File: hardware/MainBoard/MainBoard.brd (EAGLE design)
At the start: 90 x 56 mm, 220 parts, among them J1 CON-71741-2184-BOT, J2 CON-71741-2184-TOP, J3 CON-FTSH-105-01-L-DV-K, J4 CON-ZX62R-B-5P, J5 CON-SMA, J6 CON-SMA, J7 CON-RJ45-J0G-0007NL, J8 SWITCH-CJS-1200-1200, M1 MOUNT-HOLE3.3, M2 MOUNT-HOLE3.3, M3 MOUNT-HOLE3.3, M4 MOUNT-HOLE3.3, M5 FIDUCIAL1X2, M6 FIDUCIAL1X2, M7 FIDUCIAL1X2, M8 FIDUCIAL1X2, Q1 MMBT3904, SW1 SWITCH-KSC-201J, SW2 SWITCH-KSC-201J, U1 A2F500M3G-FG256, U2 MAX19706-T4877-4, U3 MAX19706-T4877-4, U4 USBLC6-2SC6, U5 FT232HL, U6 DP83848C-VBH48A, U7 93LC56BT-OT, U8 DS1818-10-SOT-23, U9 LMV112, X1 FOX924B, X2 ECX-31B, X3 ASEM1-C, X5 ECX-42-120

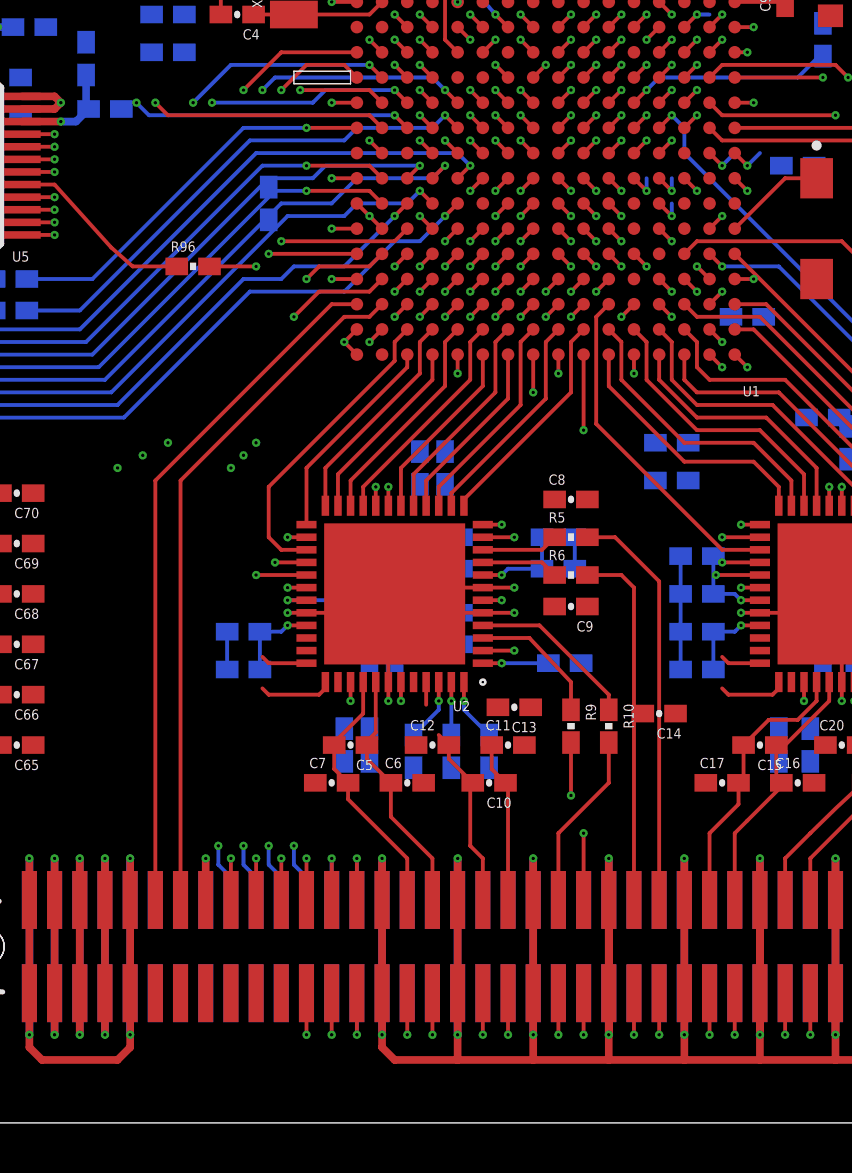
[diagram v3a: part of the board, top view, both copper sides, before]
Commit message: 
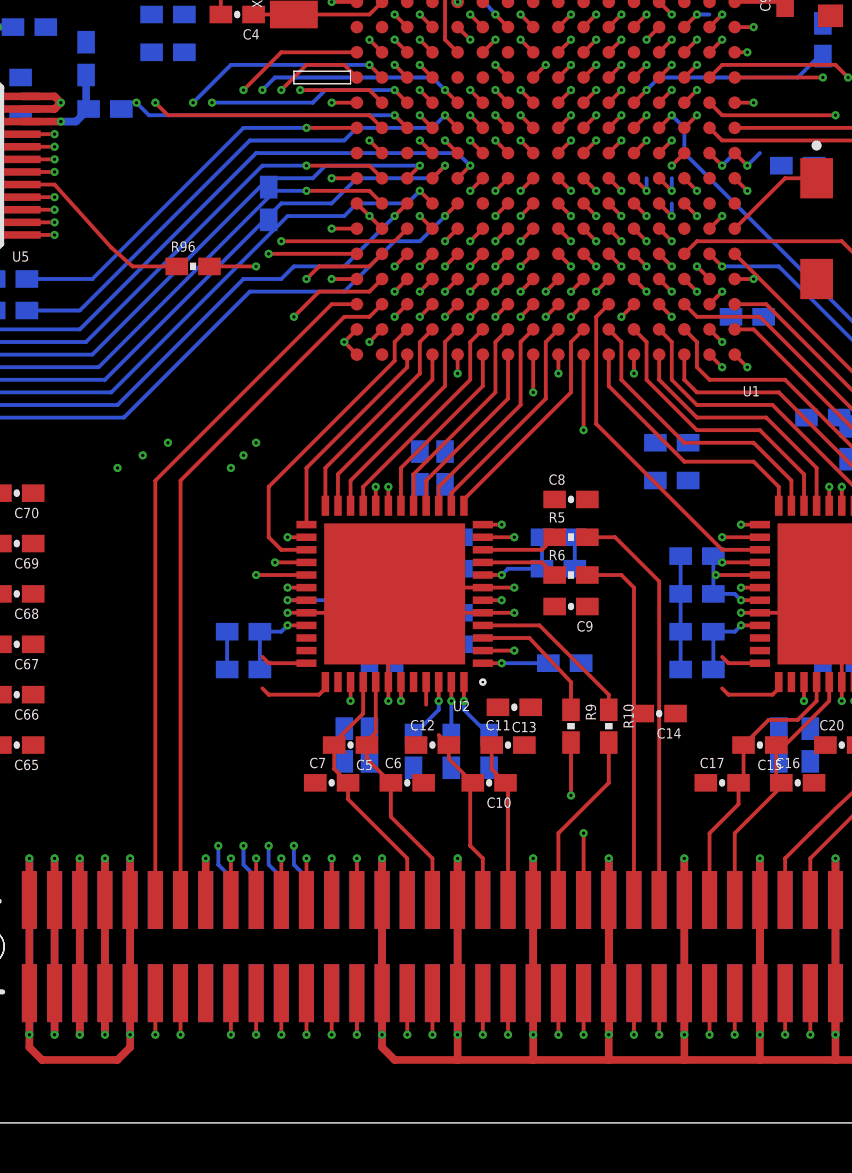
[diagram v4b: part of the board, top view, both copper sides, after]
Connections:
- removed net N$6: U1.G5
- net NGPIO0: now also U1.J3
- net NGPIO1: now also U1.H2
- net NGPIO2: now also U1.G1
- net NGPIO3: now also U1.G3
- net NGPIO4: now also U1.G2
- net SGPIO0: now also U1.E4
- net SGPIO1: now also U1.F5
- net SGPIO2: now also U1.D5
- net SGPIO3: now also U1.G5
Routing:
- net NGPIO0: track 0.00 -> 6.39 mm, vias 0 -> 2
- net NGPIO2: track 0.00 -> 5.19 mm, vias 0 -> 1
- net NGPIO1: track 0.00 -> 5.19 mm, vias 0 -> 1
- net NGPIO3: track 0.00 -> 4.98 mm, vias 0 -> 2
- net NGPIO4: track 0.00 -> 3.77 mm, vias 0 -> 1
- net SGPIO3: track 0.00 -> 1.21 mm, vias 0 -> 1
- net SGPIO2: track 0.00 -> 1.21 mm, vias 0 -> 1
- net SGPIO1: track 0.00 -> 1.21 mm, vias 0 -> 1
- net SGPIO0: track 0.00 -> 1.21 mm, vias 0 -> 1

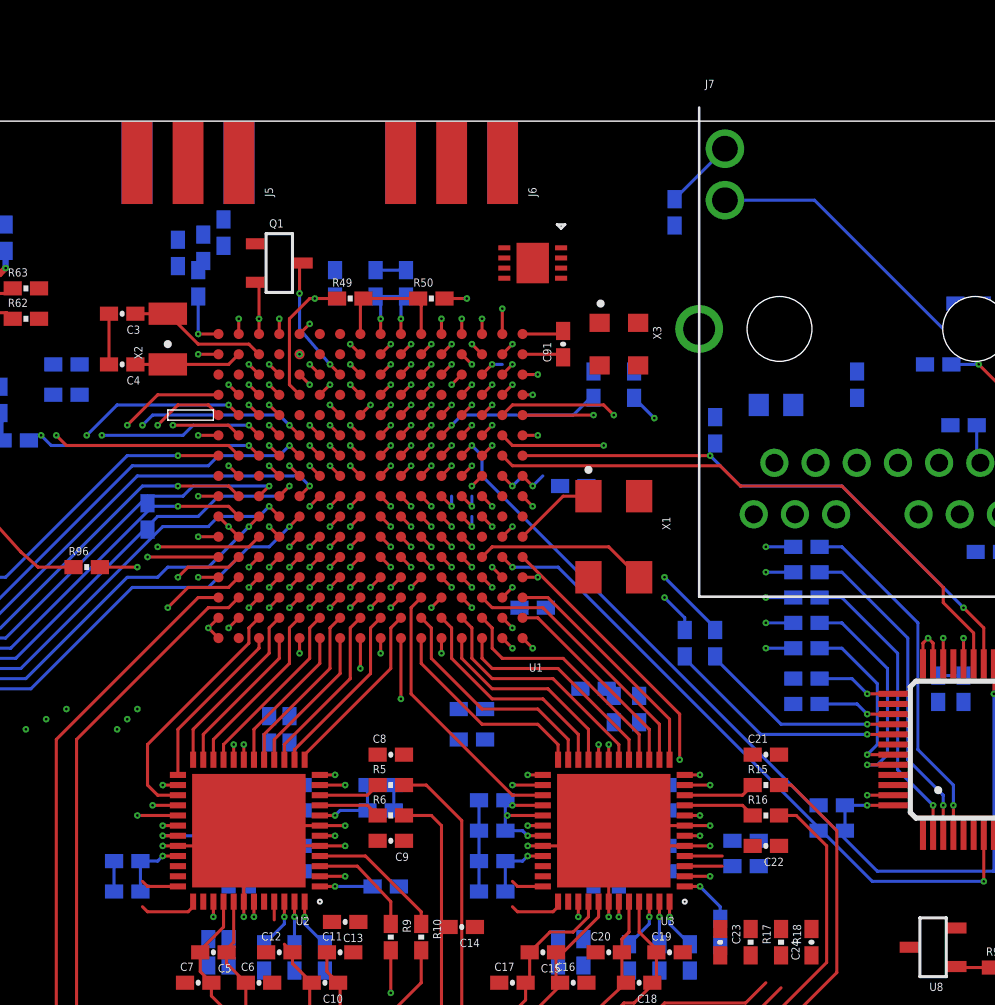
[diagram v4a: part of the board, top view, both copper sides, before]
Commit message: Routed external clocks (still needs adjustment).
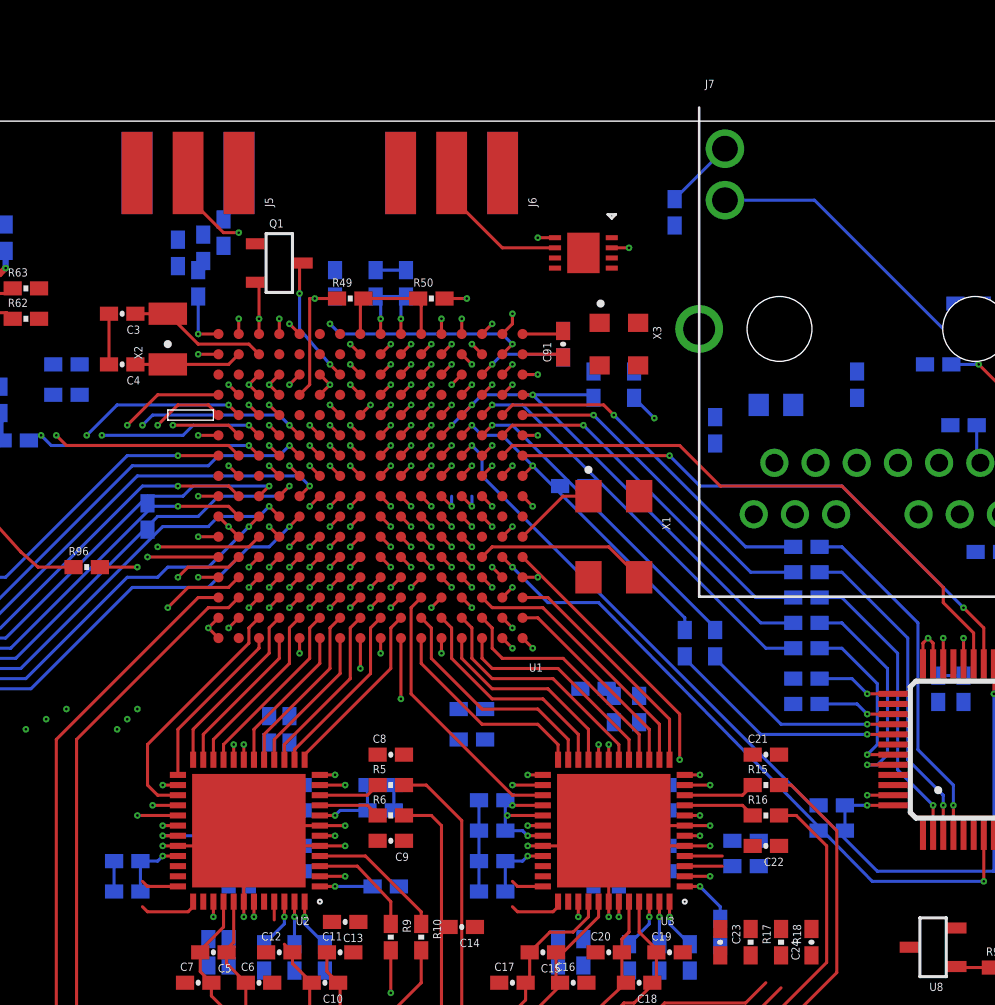
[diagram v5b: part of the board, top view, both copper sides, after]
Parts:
- moved C109 13.1 mm to (54.5, 45.0), turned to 90 degrees
- moved U9 2.55 mm to (55.5, 49.5)
- moved J5 0.50 mm to (36.0, 55.5)
- moved J6 0.50 mm to (49.0, 55.5)
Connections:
- net D3V3: no longer C74.1, C75.1, C76.1
- net VJTAG: now also C74.1
- net VPUMP: now also C75.1, C76.1
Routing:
- net EXT_CLK_IN: track 1.21 -> 30.2 mm, vias 1 -> 2
- net EXT_CLK_OUT: track 1.41 -> 14.2 mm, vias 1 -> 2
- net EXT_CLK_OUT_EN: track 1.41 -> 13.3 mm, vias 1 -> 2
- net EXT_CLK_OUT_BUF: track 0.00 -> 7.33 mm
- net VCC3N: track 1.21 -> 4.48 mm
- net SF_DAC1: track 46.5 -> 45.5 mm
- net SF_DAC0: track 54.5 -> 55.3 mm
- net SF_ABPS1: track 52.1 -> 51.4 mm
- net SF_CM0: track 50.2 -> 49.6 mm
- net MAC_TXEN: track 17.7 -> 18.1 mm, vias 2 -> 1
- net MAC_TXD1: vias 2 -> 1
- net MAC_TXD0: vias 2 -> 1
- net MAC_RXER: vias 2 -> 1
- net MAC_RXD1: vias 2 -> 1
- net MAC_RXD0: vias 2 -> 1
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
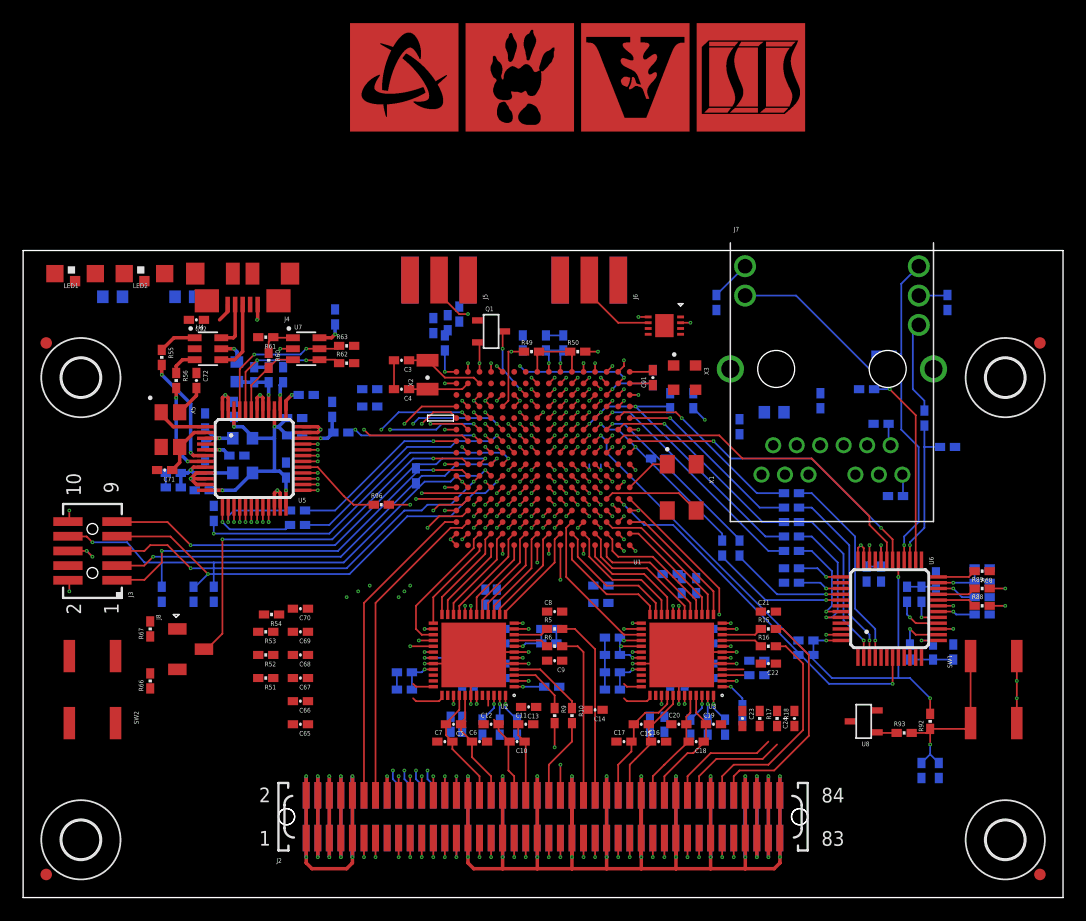
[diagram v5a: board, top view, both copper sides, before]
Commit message: 
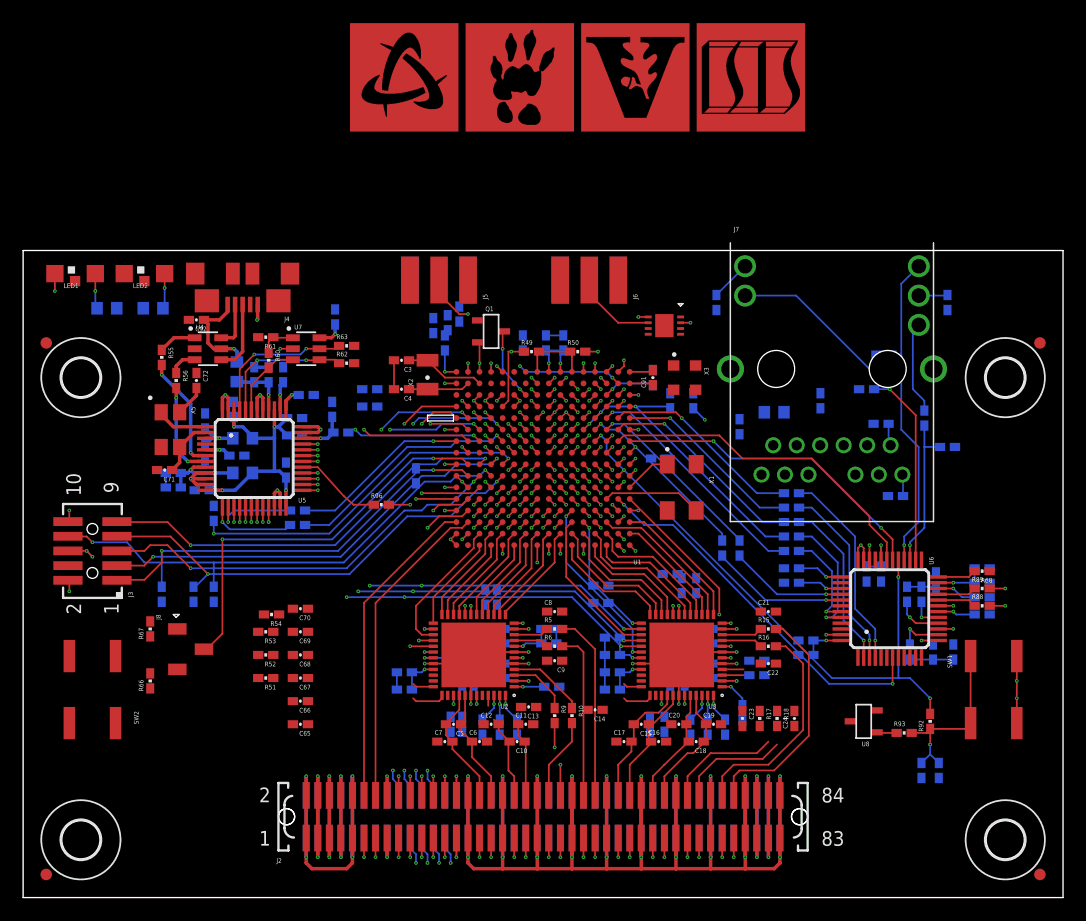
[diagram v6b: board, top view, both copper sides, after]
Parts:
- moved R98 2.93 mm to (11.2, 51.0), turned to 0 degrees
- moved R97 1.12 mm to (7.25, 51.0)
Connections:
- net NGPIO3: now also U1.D5; no longer U1.G3
- net NGPIO4: now also U1.G5; no longer U1.G2
- net SGPIO0: now also J1.25; no longer J1.23
- net SGPIO1: now also J1.23; no longer J1.21
- net SGPIO2: now also J1.21, U1.G3; no longer J1.19, U1.D5
- net SGPIO3: now also J1.19, U1.G2; no longer J1.17, U1.G5
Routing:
- net LED1: track 1.21 -> 59.0 mm, vias 1 -> 2
- net LED2: track 1.21 -> 52.5 mm
- net NGPIO4: track 3.77 -> 47.5 mm, vias 1 -> 2
- net NGPIO0: track 6.39 -> 48.8 mm
- net NGPIO3: track 4.98 -> 44.1 mm
- net NGPIO1: track 5.19 -> 39.2 mm, vias 1 -> 2
- net NGPIO2: track 5.19 -> 35.6 mm, vias 1 -> 2
- net SGPIO3: track 1.21 -> 10.3 mm, vias 1 -> 2
- net SGPIO2: track 1.21 -> 9.27 mm, vias 1 -> 2
- net SGPIO1: track 1.21 -> 9.27 mm, vias 1 -> 2
- net AFE1_CLK: track 12.4 -> 19.2 mm
- net SGPIO0: track 1.21 -> 7.27 mm, vias 1 -> 2
- net VBUS: track 3.97 -> 8.82 mm
- net DGND: track 115.5 -> 119.9 mm, vias 67 -> 68
- net N$79: track 0.00 -> 3.06 mm, vias 0 -> 1
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
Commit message: 
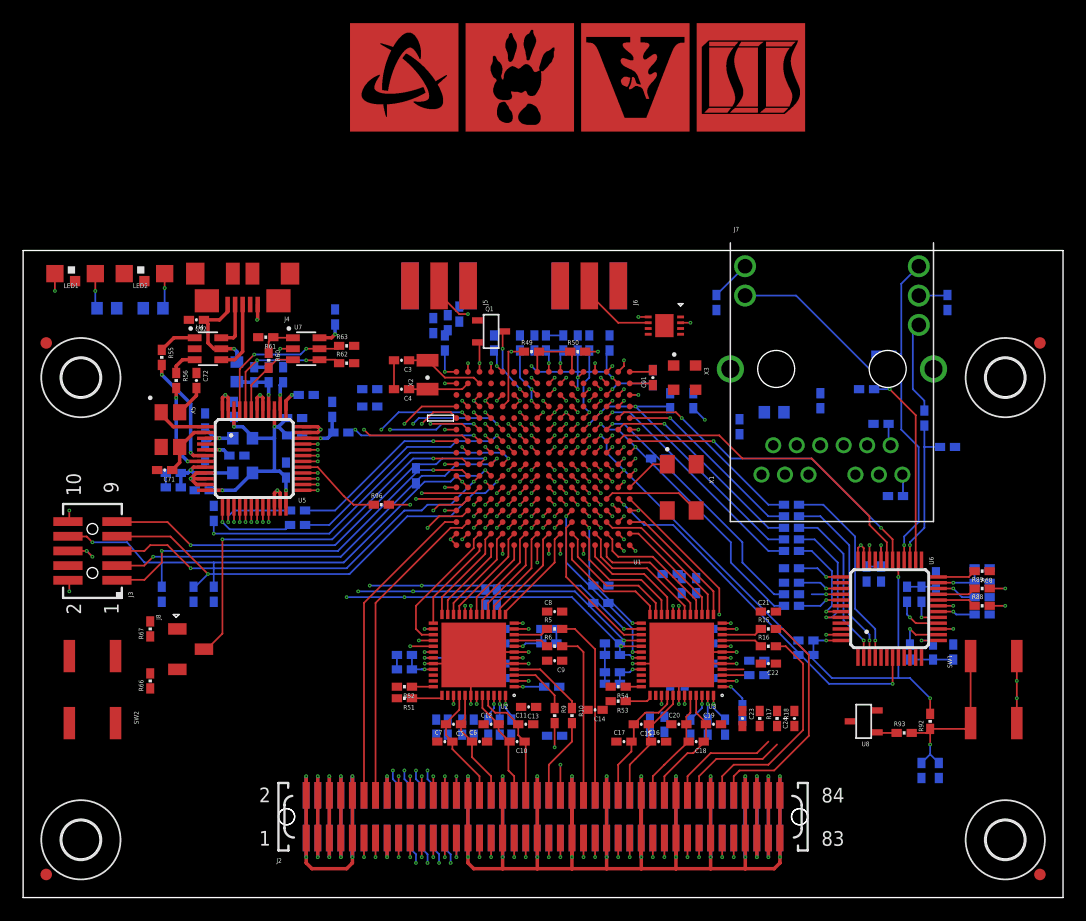
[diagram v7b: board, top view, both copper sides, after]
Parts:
- moved C66 40.9 mm to (50.8, 48.0), flipped to the bottom, turned to 90 degrees
- moved C67 37.6 mm to (48.0, 48.0), flipped to the bottom, turned to 90 degrees
- moved C65 37.0 mm to (40.8, 48.0), flipped to the bottom, turned to 90 degrees
- moved C68 36.8 mm to (49.0, 48.0), flipped to the bottom, turned to 90 degrees
- moved C69 31.4 mm to (43.0, 48.0), flipped to the bottom, turned to 90 degrees
- moved R53 31.1 mm to (51.5, 17.0)
- moved R54 30.6 mm to (51.5, 18.2)
- moved C70 24.6 mm to (46.0, 14.0), flipped to the bottom, turned to 0 degrees
- moved R52 12.3 mm to (33.0, 18.2)
- moved R51 12.1 mm to (33.0, 17.2)
- moved R78 7.81 mm to (66.5, 25.2), turned to 180 degrees
- moved R86 6.02 mm to (66.5, 26.2), turned to 180 degrees
- moved C38 4.37 mm to (39.0, 14.8), turned to 270 degrees
- moved C39 4.37 mm to (38.0, 14.8), turned to 90 degrees
- moved C34 1.75 mm to (33.0, 19.8)
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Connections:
- net NGPIO0: now also U1.G3; no longer U1.J3
- net NGPIO1: now also U1.E4; no longer U1.H2
- net NGPIO2: now also U1.F5; no longer U1.G1
- net SF_ADC1: now also R54.2; no longer R51.2
- net SF_ADC3: now also R53.2; no longer R52.2
- net SF_ADC5: now also R52.2; no longer R53.2
- net SF_ADC7: now also R51.2; no longer R54.2
- net SGPIO0: now also U1.H2; no longer U1.E4
- net SGPIO1: now also U1.G1; no longer U1.F5
- net SGPIO2: now also U1.J3; no longer U1.G3
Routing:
- net SGPIO2: track 9.27 -> 49.0 mm
- net SGPIO3: track 10.3 -> 46.5 mm
- net SGPIO0: track 7.27 -> 41.0 mm
- net SGPIO1: track 9.27 -> 39.8 mm
- net MAC_RXER: track 15.7 -> 24.1 mm
- net RX_ER: track 11.9 -> 3.86 mm
- net NGPIO2: track 35.6 -> 43.6 mm
- net CRS: track 10.2 -> 2.55 mm
- net MAC_CRS: track 15.9 -> 22.7 mm
- net NGPIO0: track 48.8 -> 42.6 mm
- net SF_ADC3: track 40.0 -> 45.7 mm
- net SF_ADC5: track 42.5 -> 47.2 mm
- net SF_ADC1: track 43.2 -> 46.6 mm
- net DAC2+: track 7.32 -> 10.6 mm
- net NGPIO1: track 39.2 -> 42.4 mm
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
